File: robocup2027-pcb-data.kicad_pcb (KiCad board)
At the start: 4 copper layers, 83 x 117 mm, 52 parts, among them M5 Motor_Servo, M6 Motor_Servo, Q1 BPW40, Q2 BPW40, U1 ESP32-DEVKITC-32E

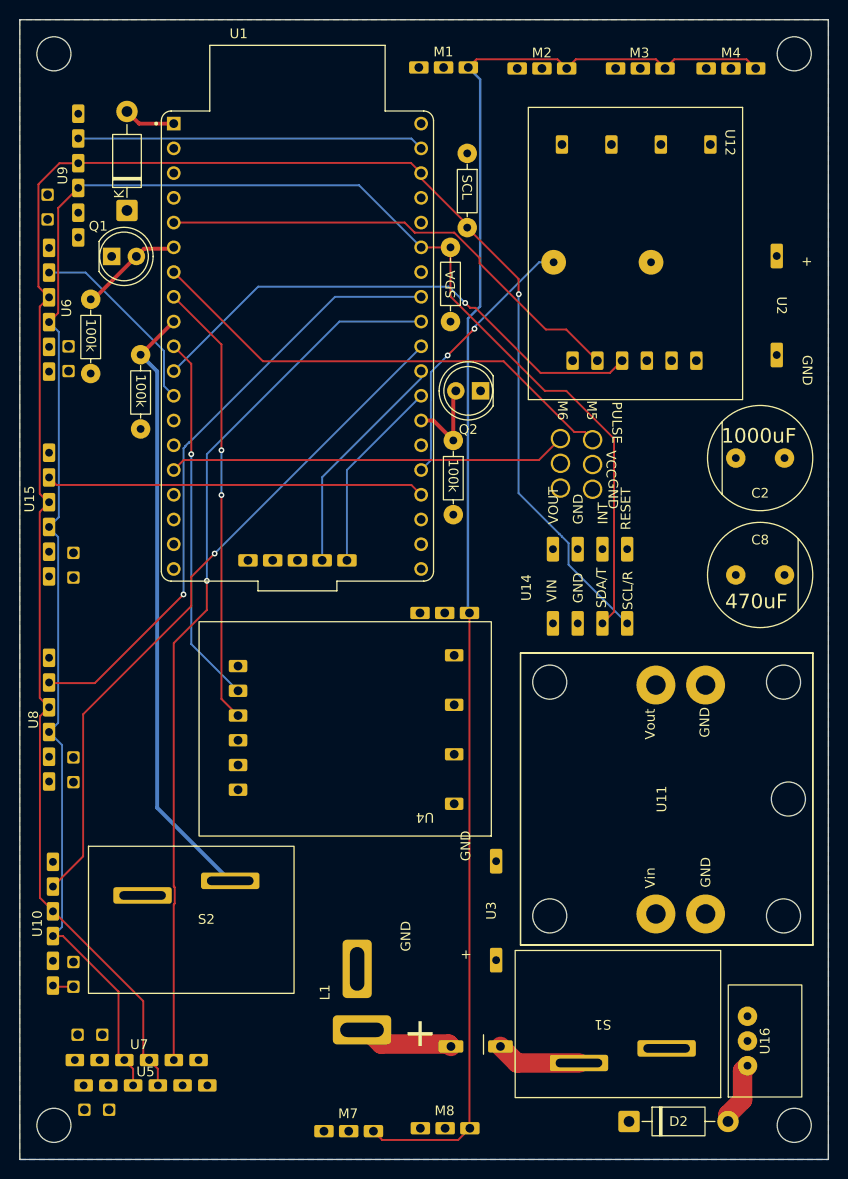
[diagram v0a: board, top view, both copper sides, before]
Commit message: two ground layers
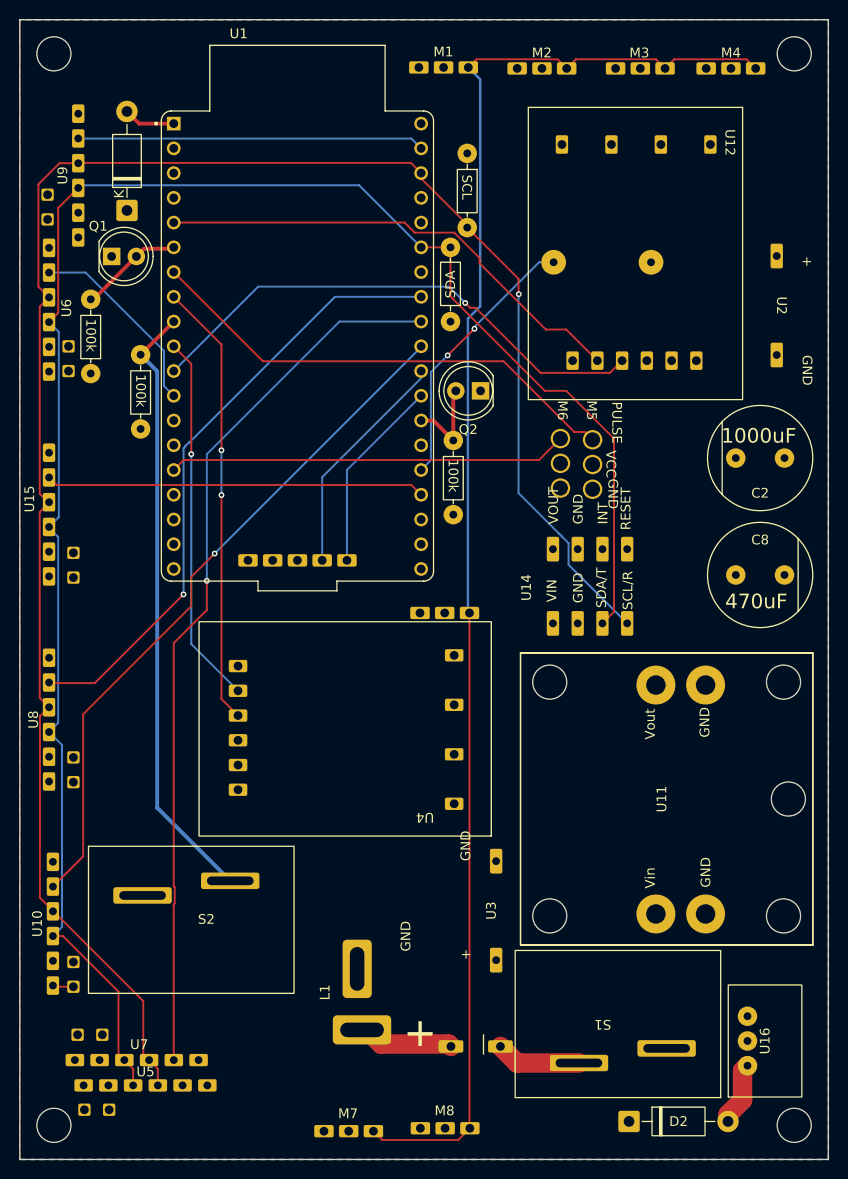
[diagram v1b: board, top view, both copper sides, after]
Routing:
- added copper zone on F.Cu, net GND
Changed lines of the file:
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@@
+	)
+	(zone
+		(net 2)
+		(net_name "GND")
+		(layer "F.Cu")
+		(hatch edge 0.5)
+		(connect_pads
+			(clearance 0.5)
+		)
+		(min_thickness 0.25)
+		(filled_areas_thickness no)
+		(fill yes
+			(thermal_gap 0.5)
+			(thermal_bridge_width 0.5)
+		)
+		(polygon
+			(pts
+				(xy 90 33.01) (xy 89.99 150.01) (xy 173.01 150.01) (xy 173 32.99)
+			)
+		)
 	)
 	(zone
